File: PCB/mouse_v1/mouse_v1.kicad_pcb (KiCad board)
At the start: 2 copper layers, 90 x 100 mm, 61 parts, among them IC1 NJM7805FA, IC2 SIT2001BI-S2-33E-12.000000G, J1 Conn_01x06_Socket, J2 Conn_01x06_Socket, J3 Conn_01x02_Socket, Q1 2SC1815GRTE2FT, Q2 2SJ681_Q_, Q3 2SJ681_Q_, Q4 ST-1KL3A, Q5 ST-1KL3A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

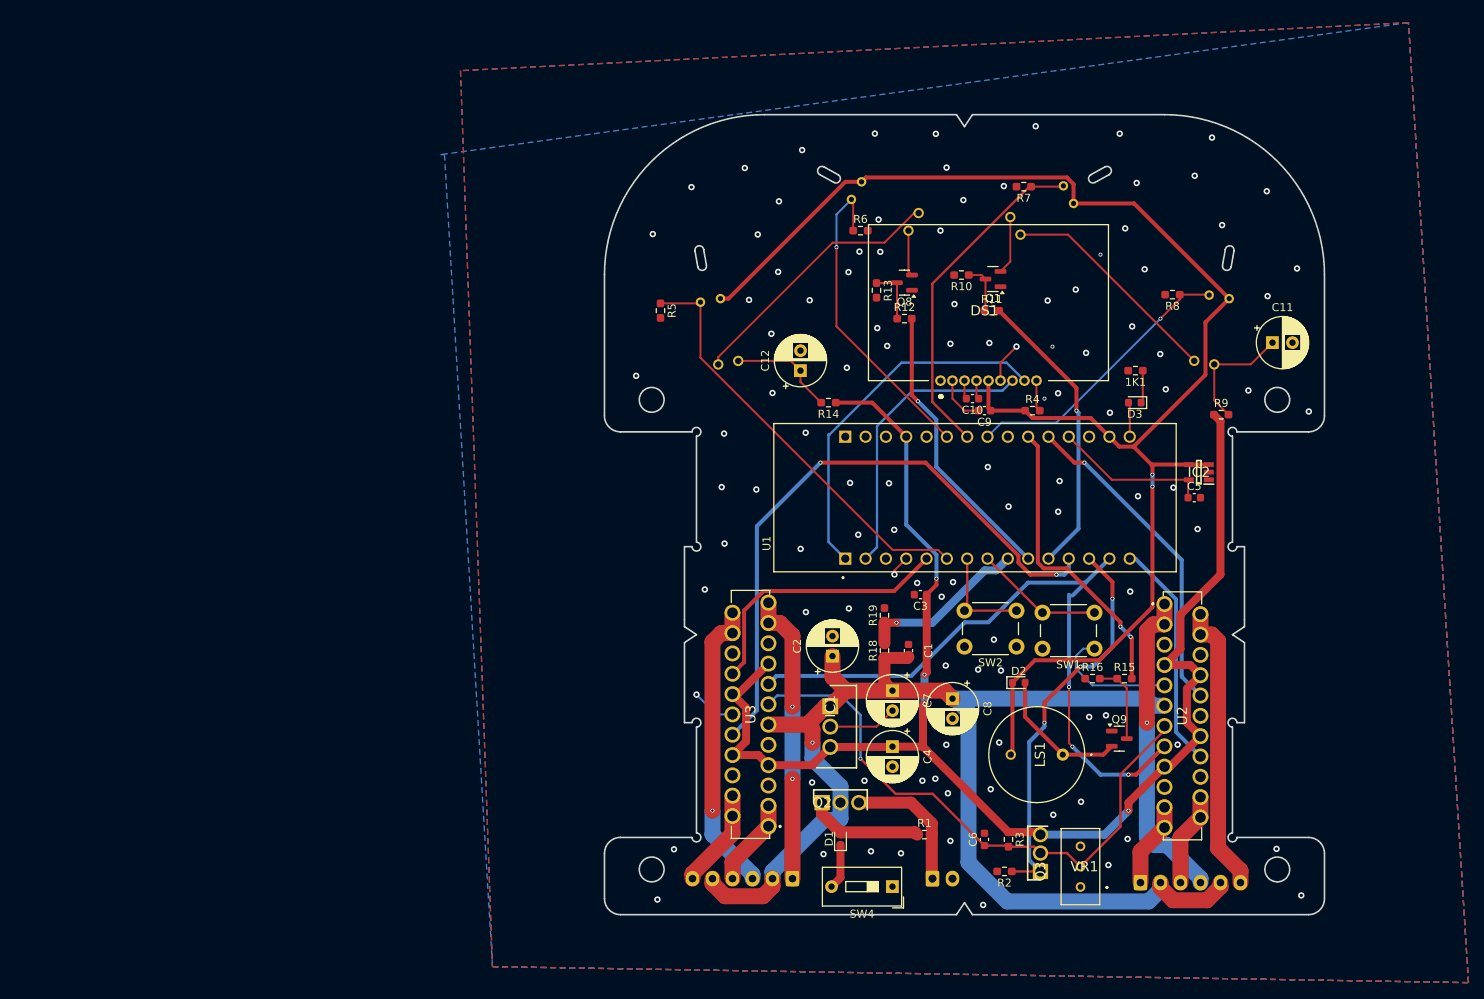
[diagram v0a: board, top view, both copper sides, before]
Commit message: LEDのコンデンサ部分の配線を太くした
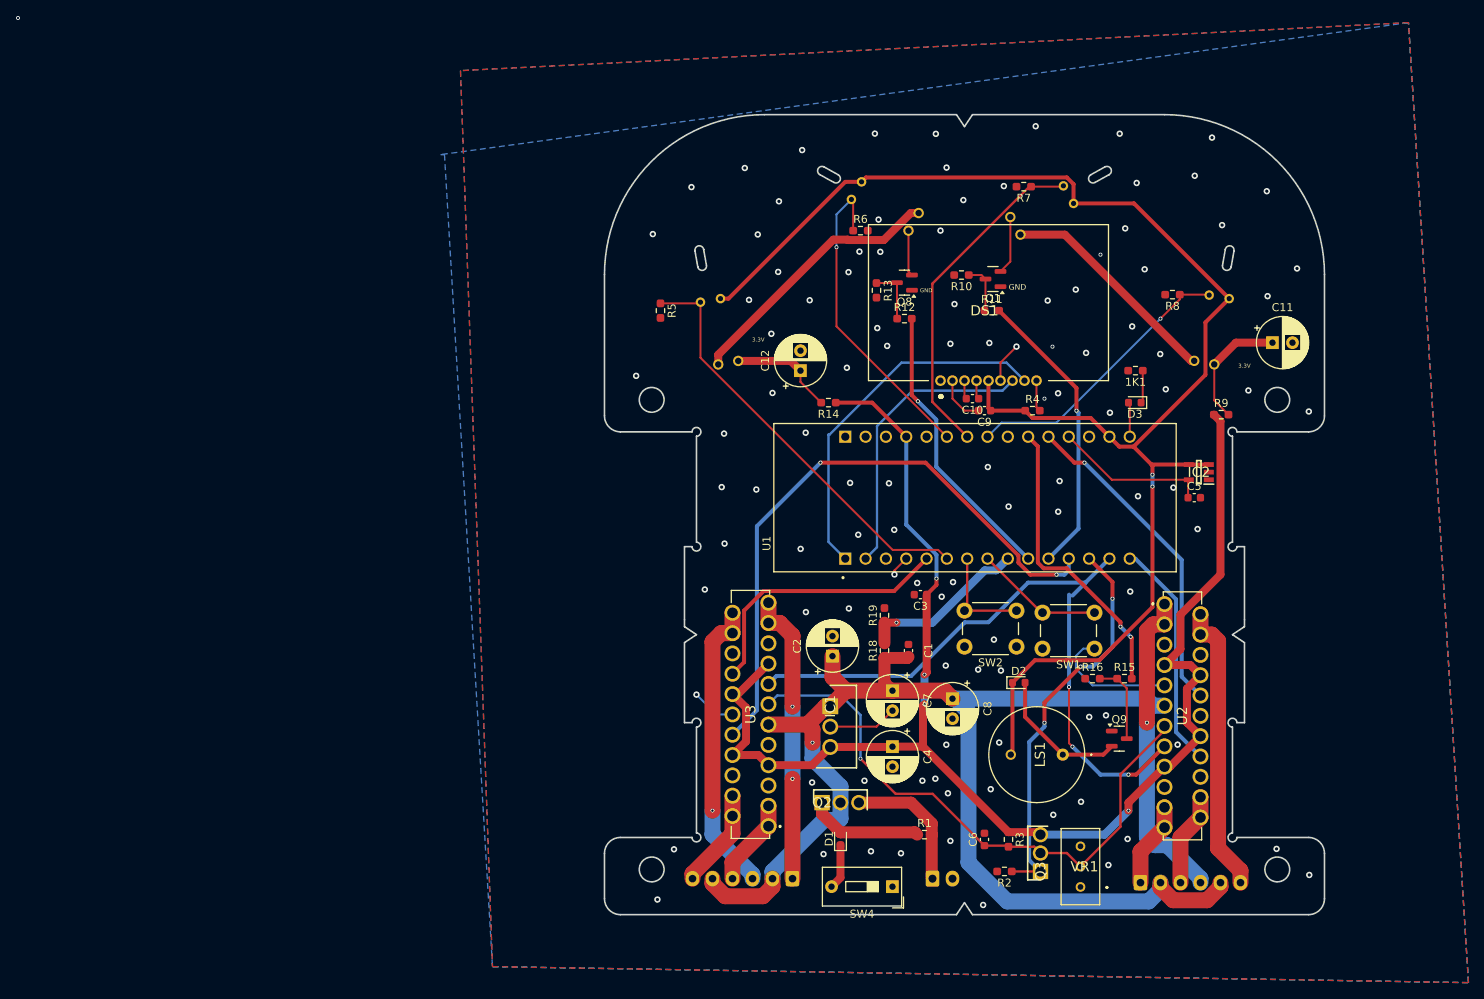
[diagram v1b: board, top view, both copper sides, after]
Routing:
- net (no net): vias 0 -> 1
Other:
- board text added: "3.3V"
- board text added: "GND"
